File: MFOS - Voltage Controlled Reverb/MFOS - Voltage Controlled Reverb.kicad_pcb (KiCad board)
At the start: 2 copper layers, 0 parts

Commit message: placed components on pcb, some caps i think have the wrong footprint
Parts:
- added C1: 1uF, Capacitor_THT:C_Rect_L7.0mm_W2.5mm_P5.00mm, F.Cu at (165.0, 54.7)
- added C10: 1uF, Capacitor_THT:C_Rect_L7.0mm_W2.5mm_P5.00mm, F.Cu at (152.1, 40.4)
- added C11: 1uF, Capacitor_THT:C_Rect_L7.0mm_W2.5mm_P5.00mm, F.Cu at (170.9, 37.3)
- added C12: 1uF, Capacitor_THT:C_Rect_L7.0mm_W2.5mm_P5.00mm, F.Cu at (171.9, 22.6)
- added C13: 1uF, Capacitor_THT:C_Rect_L7.0mm_W2.5mm_P5.00mm, F.Cu at (164.7, 45.6)
- added C14: 0.01uF, Capacitor_THT:C_Rect_L7.0mm_W2.5mm_P5.00mm, F.Cu at (80.7, 83.4)
- added C15: 0.1uF, Capacitor_THT:C_Rect_L7.0mm_W2.5mm_P5.00mm, F.Cu at (111.0, 54.2)
- added C16: 0.1uF, Capacitor_THT:C_Rect_L7.0mm_W2.5mm_P5.00mm, F.Cu at (29.5, 90.2)
- added C17: 0.1uF, Capacitor_THT:C_Rect_L7.0mm_W2.5mm_P5.00mm, F.Cu at (61.9, 89.9)
- added C18: 0.1uF, Capacitor_THT:C_Rect_L7.0mm_W2.5mm_P5.00mm, F.Cu at (53.9, 57.0)
- added C19: 0.1uF, Capacitor_THT:C_Rect_L7.0mm_W2.5mm_P5.00mm, F.Cu at (87.7, 27.5)
- added C2: 100pF, Capacitor_THT:C_Rect_L7.0mm_W2.5mm_P5.00mm, F.Cu at (46.6, 103.6)
- added C20: 10uF, Capacitor_THT:CP_Radial_D8.0mm_P3.50mm, F.Cu at (123.0, 58.1)
- added C21: 0.1uF, Capacitor_THT:C_Rect_L7.0mm_W2.5mm_P5.00mm, F.Cu at (113.4, 30.7)
- added C22: 0.1uF, Capacitor_THT:C_Rect_L7.0mm_W2.5mm_P5.00mm, F.Cu at (46.5, 91.7)
- added C23: 0.1uF, Capacitor_THT:C_Rect_L7.0mm_W2.5mm_P5.00mm, F.Cu at (74.4, 113.9)
- added C24: 0.1uF, Capacitor_THT:C_Rect_L7.0mm_W2.5mm_P5.00mm, F.Cu at (54.1, 41.9)
- added C25: 0.1uF, Capacitor_THT:C_Rect_L7.0mm_W2.5mm_P5.00mm, F.Cu at (81.0, 71.1)
- added C26: 10uF, Capacitor_THT:CP_Radial_D8.0mm_P3.50mm, F.Cu at (125.7, 17.2)
- added C27: 0.022uF, Capacitor_THT:C_Rect_L7.0mm_W2.5mm_P5.00mm, F.Cu at (111.1, 104.7)
- added C3: 220uF, Capacitor_THT:C_Rect_L7.0mm_W2.5mm_P5.00mm, F.Cu at (163.5, 63.6)
- added C4: 0.047uF, Capacitor_THT:C_Rect_L7.0mm_W2.5mm_P5.00mm, F.Cu at (107.7, 92.2)
- added C5: 0.1uF, Capacitor_THT:C_Rect_L7.0mm_W2.5mm_P5.00mm, F.Cu at (54.0, 84.1)
- added C6: 220uF, Capacitor_THT:CP_Radial_D8.0mm_P3.50mm, F.Cu at (129.4, 97.0)
- added C7: 220uF, Capacitor_THT:CP_Radial_D8.0mm_P3.50mm, F.Cu at (130.3, 106.9)
- added C8: 10uF, Capacitor_THT:CP_Radial_D8.0mm_P3.50mm, F.Cu at (91.8, 83.8)
- added C9: 10uF, Capacitor_THT:CP_Radial_D8.0mm_P3.50mm, F.Cu at (160.5, 28.6)
- added D1: 1N914, Diode_THT:D_T-1_P5.08mm_Horizontal, F.Cu at (25.7, 69.6)
- added D2: 1N914, Diode_THT:D_T-1_P5.08mm_Horizontal, F.Cu at (26.8, 26.1)
- added D3: 1N914, Diode_THT:D_T-1_P5.08mm_Horizontal, F.Cu at (59.4, 95.9)
- added D4: 1N914, Diode_THT:D_T-1_P5.08mm_Horizontal, F.Cu at (131.4, 75.7)
- added J1: X6, Connector_Wire:SolderWirePad_1x01_Drill1mm, F.Cu at (54.7, 109.7)
- added J10: X5, Connector_Wire:SolderWirePad_1x01_Drill1mm, F.Cu at (104.1, 76.0)
- added J11: GND_Conn, Connector_Wire:SolderWirePad_1x02_P3.81mm_Drill1mm, F.Cu at (126.8, 36.7)
- added J12: +12V_Conn, Connector_Wire:SolderWirePad_1x02_P3.81mm_Drill1mm, F.Cu at (126.8, 45.5)
- added J13: -12V_Conn, Connector_Wire:SolderWirePad_1x02_P3.81mm_Drill1mm, F.Cu at (127.9, 27.9)
- added J14: X4, Connector_Wire:SolderWirePad_1x01_Drill1mm, F.Cu at (135.6, 94.7)
- added J2: X9, Connector_Wire:SolderWirePad_1x01_Drill1mm, F.Cu at (104.5, 17.1)
- added J3: X10, Connector_Wire:SolderWirePad_1x01_Drill1mm, F.Cu at (45.8, 16.0)
- added J4: X7, Connector_Wire:SolderWirePad_1x01_Drill1mm, F.Cu at (50.9, 109.9)
- added J5: X8, Connector_Wire:SolderWirePad_1x01_Drill1mm, F.Cu at (50.3, 16.0)
- added J6: X11, Connector_Wire:SolderWirePad_1x01_Drill1mm, F.Cu at (97.2, 68.3)
- added J7: X1, Connector_Wire:SolderWirePad_1x01_Drill1mm, F.Cu at (95.6, 95.9)
- added J8: X2, Connector_Wire:SolderWirePad_1x01_Drill1mm, F.Cu at (21.5, 109.1)
- added J9: X3, Connector_Wire:SolderWirePad_1x01_Drill1mm, F.Cu at (126.8, 88.9)
- added Q1: 2N3906, Package_TO_SOT_THT:TO-92_Inline_Wide, F.Cu at (29.4, 61.4)
- added Q2: 2N3906, Package_TO_SOT_THT:TO-92_Inline_Wide, F.Cu at (29.0, 37.4)
- added R1: 1M, Resistor_THT:R_Axial_DIN0207_L6.3mm_D2.5mm_P7.62mm_Horizontal, F.Cu at (21.2, 99.5)
- added R10: 4.7K, Resistor_THT:R_Axial_DIN0207_L6.3mm_D2.5mm_P7.62mm_Horizontal, F.Cu at (87.9, 70.6)
- added R11: 43K, Resistor_THT:R_Axial_DIN0207_L6.3mm_D2.5mm_P7.62mm_Horizontal, F.Cu at (37.4, 68.1)
- added R12: 1K, Resistor_THT:R_Axial_DIN0207_L6.3mm_D2.5mm_P7.62mm_Horizontal, F.Cu at (68.6, 73.9)
- added R13: 100K, Resistor_THT:R_Axial_DIN0207_L6.3mm_D2.5mm_P7.62mm_Horizontal, F.Cu at (50.6, 70.0)
- added R14: 100K, Resistor_THT:R_Axial_DIN0207_L6.3mm_D2.5mm_P7.62mm_Horizontal, F.Cu at (42.0, 68.3)
- added R16: 47K, Resistor_THT:R_Axial_DIN0207_L6.3mm_D2.5mm_P7.62mm_Horizontal, F.Cu at (74.8, 73.6)
- added R17: 470K, Resistor_THT:R_Axial_DIN0207_L6.3mm_D2.5mm_P7.62mm_Horizontal, F.Cu at (95.1, 55.9)
- added R18: 100K, Resistor_THT:R_Axial_DIN0207_L6.3mm_D2.5mm_P7.62mm_Horizontal, F.Cu at (100.2, 55.7)
- added R19: 200K, Resistor_THT:R_Axial_DIN0207_L6.3mm_D2.5mm_P7.62mm_Horizontal, F.Cu at (69.2, 30.0)
- added R2: 6.2K, Resistor_THT:R_Axial_DIN0207_L6.3mm_D2.5mm_P7.62mm_Horizontal, F.Cu at (53.5, 101.7)
- added R20: 10K, Resistor_THT:R_Axial_DIN0207_L6.3mm_D2.5mm_P7.62mm_Horizontal, F.Cu at (88.0, 39.0)
- added R21: 270K, Resistor_THT:R_Axial_DIN0207_L6.3mm_D2.5mm_P7.62mm_Horizontal, F.Cu at (105.5, 53.4)
- added R22: 15K, Resistor_THT:R_Axial_DIN0207_L6.3mm_D2.5mm_P7.62mm_Horizontal, F.Cu at (29.4, 18.7)
- added R23: 100K, Resistor_THT:R_Axial_DIN0207_L6.3mm_D2.5mm_P7.62mm_Horizontal, F.Cu at (119.8, 36.6)
- added R24: 100K, Resistor_THT:R_Axial_DIN0207_L6.3mm_D2.5mm_P7.62mm_Horizontal, F.Cu at (120.2, 48.3)
- added R25: 43K, Resistor_THT:R_Axial_DIN0207_L6.3mm_D2.5mm_P7.62mm_Horizontal, F.Cu at (48.1, 35.3)
- added R26: 1K, Resistor_THT:R_Axial_DIN0207_L6.3mm_D2.5mm_P7.62mm_Horizontal, F.Cu at (74.0, 30.2)
- added R27: 4.7K, Resistor_THT:R_Axial_DIN0207_L6.3mm_D2.5mm_P7.62mm_Horizontal, F.Cu at (95.3, 32.7)
- added R29: 100K, Resistor_THT:R_Axial_DIN0207_L6.3mm_D2.5mm_P7.62mm_Horizontal, F.Cu at (54.2, 35.1)
- added R3: 1M, Resistor_THT:R_Axial_DIN0207_L6.3mm_D2.5mm_P7.62mm_Horizontal, F.Cu at (41.1, 101.2)
- added R30: 100K, Resistor_THT:R_Axial_DIN0207_L6.3mm_D2.5mm_P7.62mm_Horizontal, F.Cu at (59.4, 34.8)
- added R32: 47K, Resistor_THT:R_Axial_DIN0207_L6.3mm_D2.5mm_P7.62mm_Horizontal, F.Cu at (82.5, 28.6)
- added R33: 470K, Resistor_THT:R_Axial_DIN0207_L6.3mm_D2.5mm_P7.62mm_Horizontal, F.Cu at (80.9, 39.7)
- added R34: 1M, Resistor_THT:R_Axial_DIN0207_L6.3mm_D2.5mm_P7.62mm_Horizontal, F.Cu at (71.4, 85.3)
- added R35: 1M, Resistor_THT:R_Axial_DIN0207_L6.3mm_D2.5mm_P7.62mm_Horizontal, F.Cu at (91.6, 107.7)
- added R36: 2K, Resistor_THT:R_Axial_DIN0207_L6.3mm_D2.5mm_P7.62mm_Horizontal, F.Cu at (89.8, 74.9)
- added R37: 200K, Resistor_THT:R_Axial_DIN0207_L6.3mm_D2.5mm_P7.62mm_Horizontal, F.Cu at (86.4, 107.8)
- added R38: 3.3K, Resistor_THT:R_Axial_DIN0207_L6.3mm_D2.5mm_P7.62mm_Horizontal, F.Cu at (81.3, 107.6)
- added R39: 1K, Resistor_THT:R_Axial_DIN0207_L6.3mm_D2.5mm_P7.62mm_Horizontal, F.Cu at (120.3, 105.4)
- added R4: 1K, Resistor_THT:R_Axial_DIN0207_L6.3mm_D2.5mm_P7.62mm_Horizontal, F.Cu at (120.6, 75.5)
- added R40: 1K, Resistor_THT:R_Axial_DIN0207_L6.3mm_D2.5mm_P7.62mm_Horizontal, F.Cu at (113.0, 110.6)
- added R5: 1K, Resistor_THT:R_Axial_DIN0207_L6.3mm_D2.5mm_P7.62mm_Horizontal, F.Cu at (125.9, 68.0)
- added R6: 10, Resistor_THT:R_Axial_DIN0207_L6.3mm_D2.5mm_P7.62mm_Horizontal, F.Cu at (109.1, 71.5)
- added R7: 15K, Resistor_THT:R_Axial_DIN0207_L6.3mm_D2.5mm_P7.62mm_Horizontal, F.Cu at (28.5, 75.5)
- added R8: 200K, Resistor_THT:R_Axial_DIN0207_L6.3mm_D2.5mm_P7.62mm_Horizontal, F.Cu at (63.5, 73.8)
- added R9: 10K, Resistor_THT:R_Axial_DIN0207_L6.3mm_D2.5mm_P7.62mm_Horizontal, F.Cu at (117.1, 95.6)
- added U1: LM386, Package_DIP:DIP-8_W7.62mm_Socket, F.Cu at (98.2, 108.6)
- added U2: LF411, Package_DIP:DIP-8_W7.62mm_Socket, F.Cu at (28.1, 103.8)
- added U3: TL074, Package_DIP:DIP-14_W7.62mm_Socket, F.Cu at (32.1, 52.8)
- added U4: LM13700, Package_DIP:DIP-16_W7.62mm_Socket, F.Cu at (66.1, 53.2)
- added U5: TL072, Package_DIP:DIP-8_W7.62mm_Socket, F.Cu at (108.5, 39.0)
- added U6: TL072, Package_DIP:DIP-8_W7.62mm_Socket, F.Cu at (66.0, 101.8)
- added Z1: 1N5231B, Diode_THT:D_T-1_P5.08mm_Horizontal, F.Cu at (114.8, 73.5)
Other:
- board outline added: 127 x 101.6 mm

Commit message: progress on wiring
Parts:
- added REF**: MountingHole_2.5mm_Pad, MountingHole:MountingHole_2.5mm_Pad, F.Cu at (15.7, 110.0)
- added REF**: MountingHole_2.5mm_Pad, MountingHole:MountingHole_2.5mm_Pad, F.Cu at (15.7, 15.7)
- C1, C10, C11, C12, C13: footprint Capacitor_THT:C_Rect_L7.0mm_W2.5mm_P5.00mm -> Capacitor_THT:CP_Radial_D5.0mm_P2.50mm
- C26, C6, C7, C8, C9: footprint Capacitor_THT:CP_Radial_D8.0mm_P3.50mm -> Capacitor_THT:CP_Radial_D6.3mm_P2.50mm
- C3: footprint Capacitor_THT:C_Rect_L7.0mm_W2.5mm_P5.00mm -> Capacitor_THT:CP_Radial_D6.3mm_P2.50mm
- moved C3 97.6 mm to (75.9, 106.7), turned to 190 degrees
- moved C12 85.3 mm to (87.9, 37.6), turned to 220 degrees
- moved C10 62.6 mm to (92.5, 59.4), turned to 180 degrees
- moved C11 58.8 mm to (112.8, 46.0)
- moved C9 55.6 mm to (111.0, 54.1), turned to 270 degrees
- moved C1 54.0 mm to (116.8, 79.0), turned to 130 degrees
- moved C13 48.2 mm to (118.4, 32.5)
- moved J1 44.5 mm to (51.6, 65.3), turned to 30 degrees
- moved J4 41.1 mm to (45.5, 69.1), turned to 30 degrees
- moved C6 37.1 mm to (122.9, 60.5), turned to 90 degrees
- moved J6 35.6 mm to (62.0, 73.9), turned to 50 degrees
- moved J8 35.5 mm to (21.2, 73.6), turned to 310 degrees
- moved R35 34.9 mm to (56.9, 104.1), turned to 320 degrees
- moved R1 33.8 mm to (29.4, 66.7), turned to 220 degrees
- moved J7 31.3 mm to (66.8, 108.2)
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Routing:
- net Earth: track 0.00 -> 349.2 mm
- net +12V: track 0.00 -> 156.2 mm
- net -12V: track 0.00 -> 151.9 mm
- net Net-(Q2-Pad3): track 0.00 -> 72.7 mm
- net Net-(R18-Pad2): track 0.00 -> 36.2 mm
- net Net-(R12-Pad2): track 0.00 -> 35.8 mm
- net Net-(C27-Pad1): track 0.00 -> 33.9 mm
- net Net-(C9-Pad1): track 0.00 -> 27.4 mm
- net Net-(C3-Pad1): track 0.00 -> 26.4 mm
- net Net-(R16-Pad2): track 0.00 -> 25.8 mm
- net Net-(C2-Pad2): track 0.00 -> 23.9 mm
- net Net-(R37-Pad1): track 0.00 -> 22.8 mm
- net Net-(C14-Pad2): track 0.00 -> 20.7 mm
- net Net-(R11-Pad2): track 0.00 -> 20.2 mm
- net LVS: track 0.00 -> 19.9 mm
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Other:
- net class Default: trace_width 0.4 -> 0.5

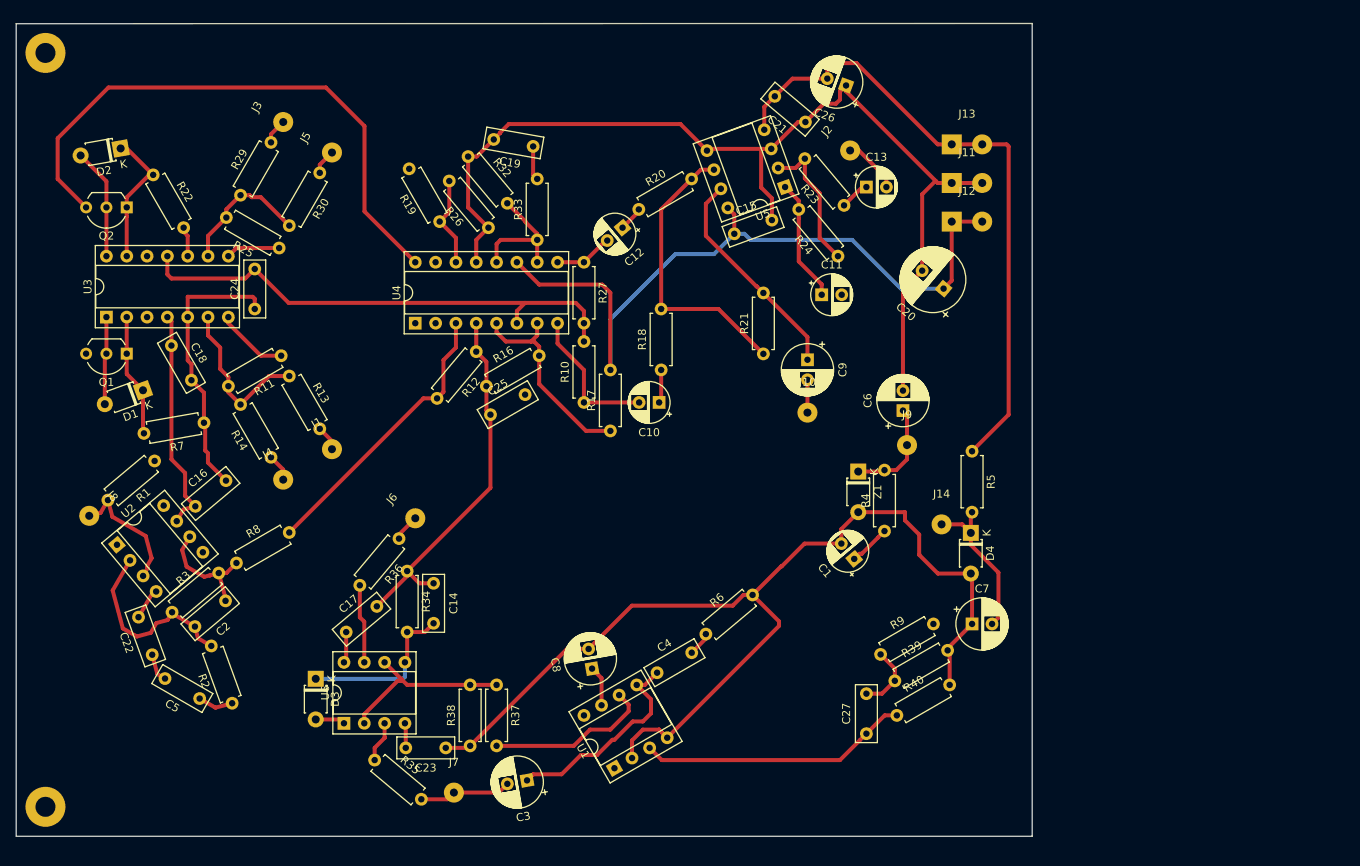
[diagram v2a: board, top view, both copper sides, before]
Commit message: finished back copper connections
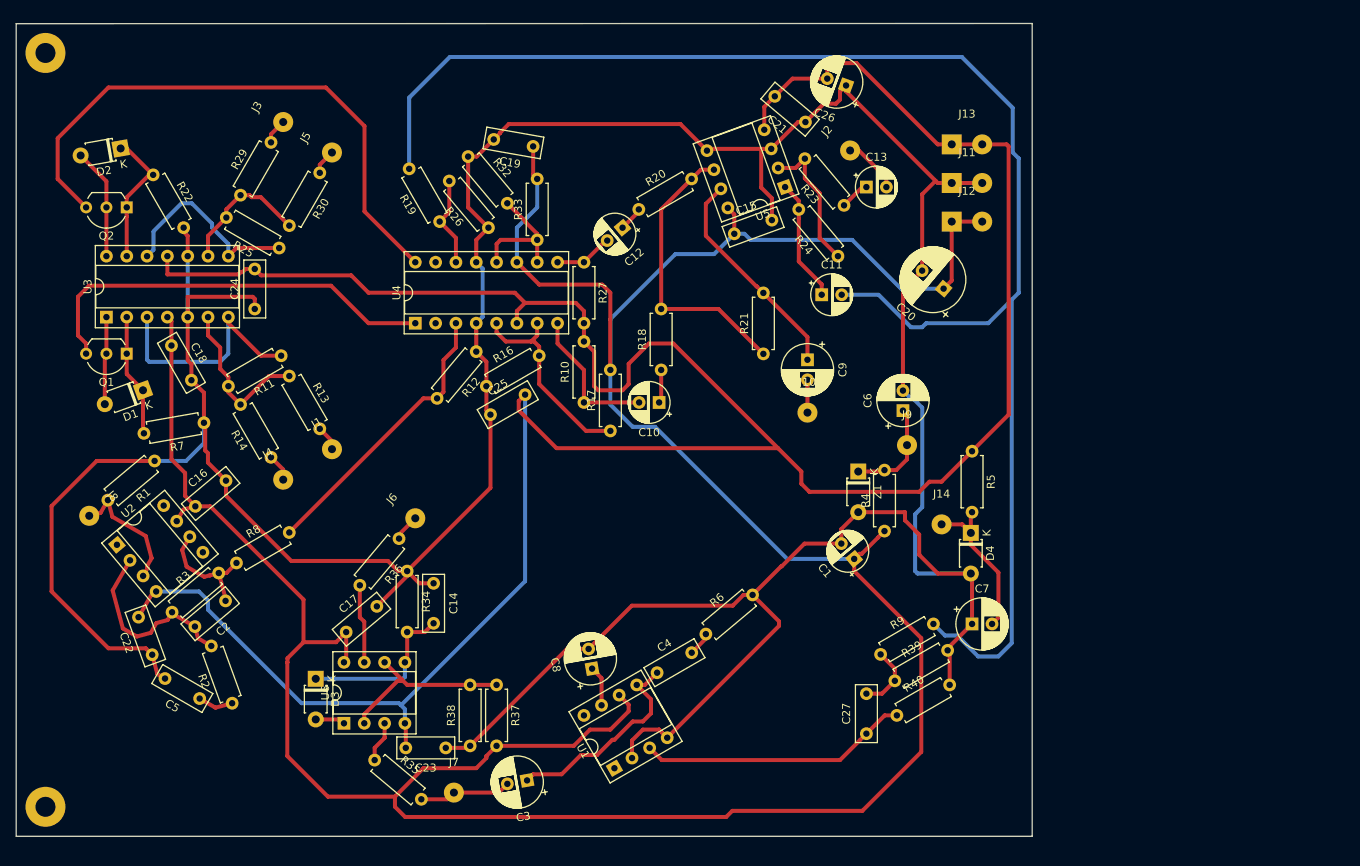
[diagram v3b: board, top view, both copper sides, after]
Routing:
- net +12V: track 156.2 -> 384.7 mm
- net Net-(C11-Pad2): track 0.00 -> 193.2 mm
- net -12V: track 151.9 -> 341.2 mm
- net Earth: track 349.2 -> 476.1 mm
- net Net-(Q1-Pad3): track 0.00 -> 52.2 mm
- net Net-(R11-Pad1): track 9.05 -> 29.6 mm
- net Net-(R25-Pad1): track 6.77 -> 24.9 mm

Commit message: probably changed some stuff idk
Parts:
- removed the REF** at (15.7, 110.0)
- removed the REF** at (15.7, 15.7)
- added REF**: MountingHole_3.5mm_Pad, MountingHole:MountingHole_3.5mm_Pad, F.Cu at (18.3, 106.7)
- added REF**: MountingHole_3.5mm_Pad, MountingHole:MountingHole_3.5mm_Pad, F.Cu at (18.3, 18.0)
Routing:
- net +12V: track 384.7 -> 383.9 mm
- net -12V: track 341.2 -> 341.7 mm
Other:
- board text added: "+12V"
- board text added: "-12V"
- board text added: "GND"
- board text added: "X1"
- board text added: "X10"
- board text added: "X11"
- board text added: "X2"
- board text added: "X3"
- board text added: "X4"
- board text added: "X5"
- board text added: "X6"
- board text added: "X7"
- board text added: "X8"
- board text added: "X9"

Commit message: uwu
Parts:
- moved C27 19.2 mm to (100.6, 93.7), turned to 70 degrees
- moved R40 18.1 mm to (104.9, 92.8), turned to 10 degrees
- moved R39 16.7 mm to (106.2, 88.7), turned to 10 degrees
- moved R9 15.7 mm to (105.6, 85.0), turned to 10 degrees
- moved C7 14.0 mm to (117.7, 85.3), turned to 340 degrees
- moved C14 10.8 mm to (66.5, 71.4)
- moved C17 10.8 mm to (55.6, 77.5)
- moved C3 10.8 mm to (78.2, 96.1)
- moved C4 10.8 mm to (94.5, 82.6)
- moved D3 10.8 mm to (51.8, 83.4)
- moved R37 10.8 mm to (74.4, 84.1)
- moved U1 10.8 mm to (89.1, 94.6)
- moved J6 10.8 mm to (64.2, 63.3)
- moved C23 10.8 mm to (68.0, 92.0)
- moved C8 10.8 mm to (86.3, 82.1)
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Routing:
- net +12V: track 383.9 -> 275.1 mm
- net -12V: track 341.7 -> 293.7 mm
- net Net-(C27-Pad1): track 33.9 -> 12.1 mm
- net Earth: track 476.1 -> 465.5 mm
- net LVS: track 19.9 -> 29.7 mm
- net Net-(C11-Pad2): track 193.2 -> 184.6 mm
- net Net-(R18-Pad2): track 36.2 -> 28.1 mm
- net Net-(C9-Pad1): track 27.4 -> 21.6 mm
- net Net-(C2-Pad2): track 23.9 -> 27.3 mm
- net Net-(C3-Pad1): track 26.4 -> 23.5 mm
- net Net-(Q1-Pad3): track 52.2 -> 50.0 mm
- net Net-(Q2-Pad3): track 72.7 -> 70.8 mm
- net Net-(C2-Pad1): track 14.8 -> 16.6 mm
- net Net-(R11-Pad2): track 20.2 -> 18.9 mm
- net Net-(R23-Pad2): track 17.7 -> 16.4 mm
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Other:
- board text removed: "X2"
